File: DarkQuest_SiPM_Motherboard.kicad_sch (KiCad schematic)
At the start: 46 parts, among them J1 Conn_Coaxial, J10 Conn_Coaxial, J11 Conn_Coaxial, J12 Conn_Coaxial, J13 8-102202-4, J14 8-102202-4, J15 8-102202-4, J16 8-102202-4, J17 SiPM Chip Pin Header (K), J18 SiPM Chip Pin Header (K)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

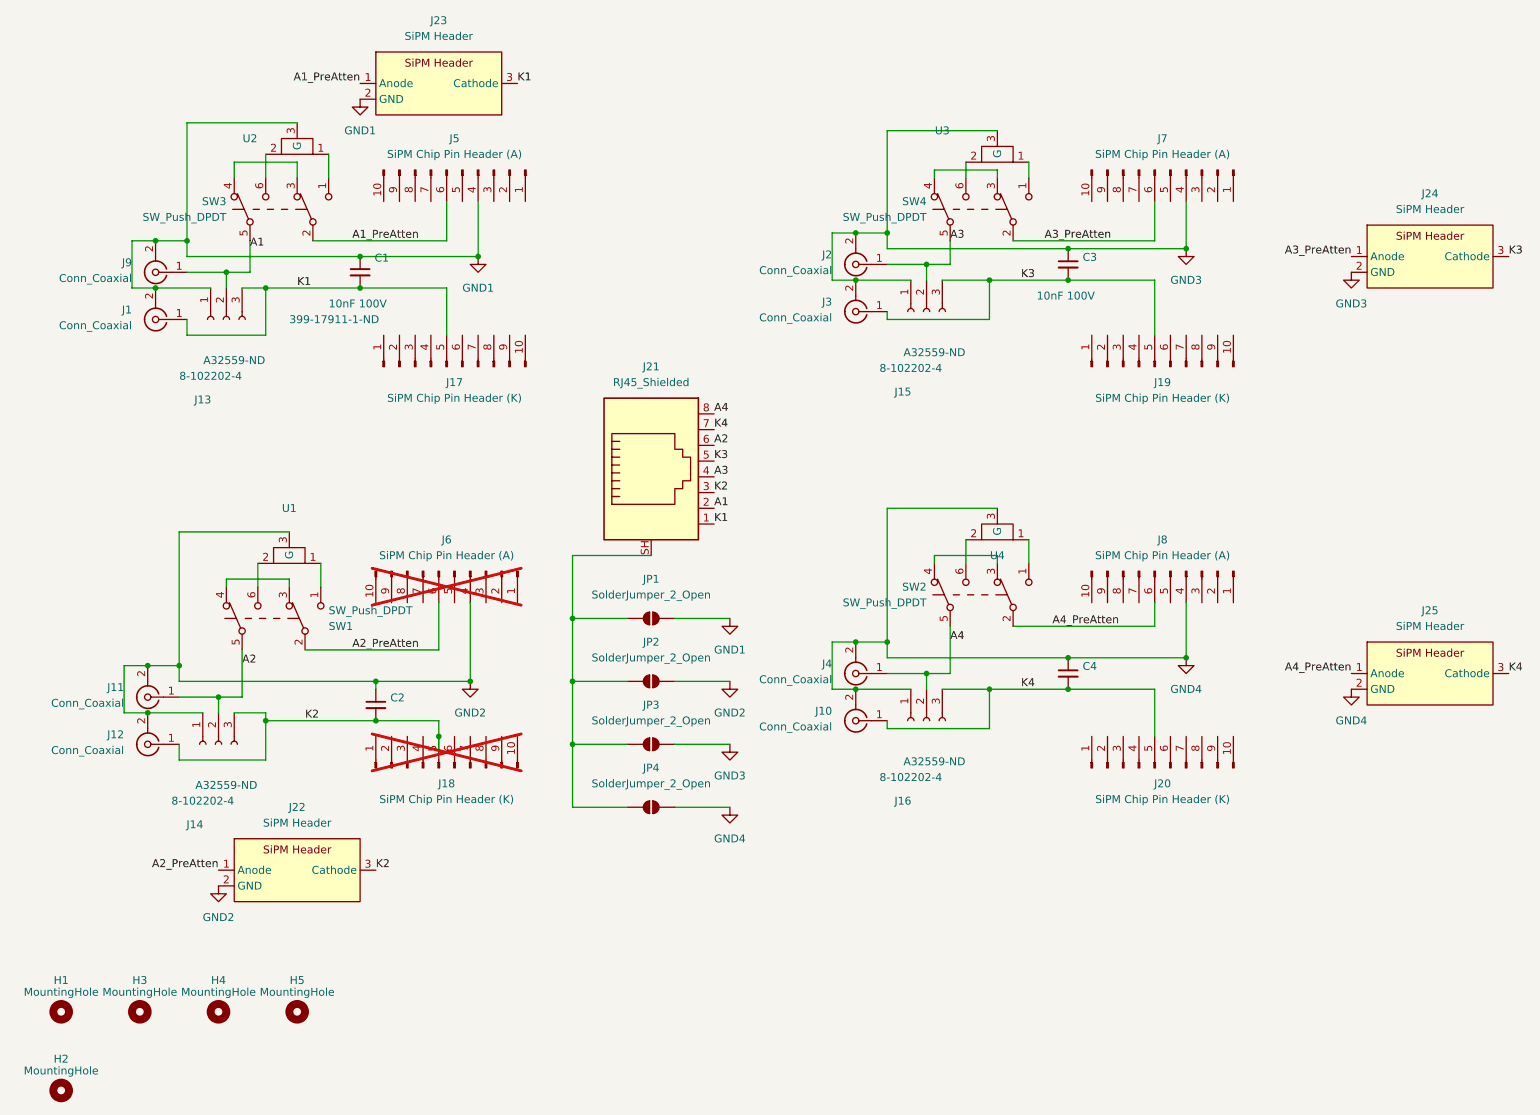
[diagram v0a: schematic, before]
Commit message: Added HDMI option
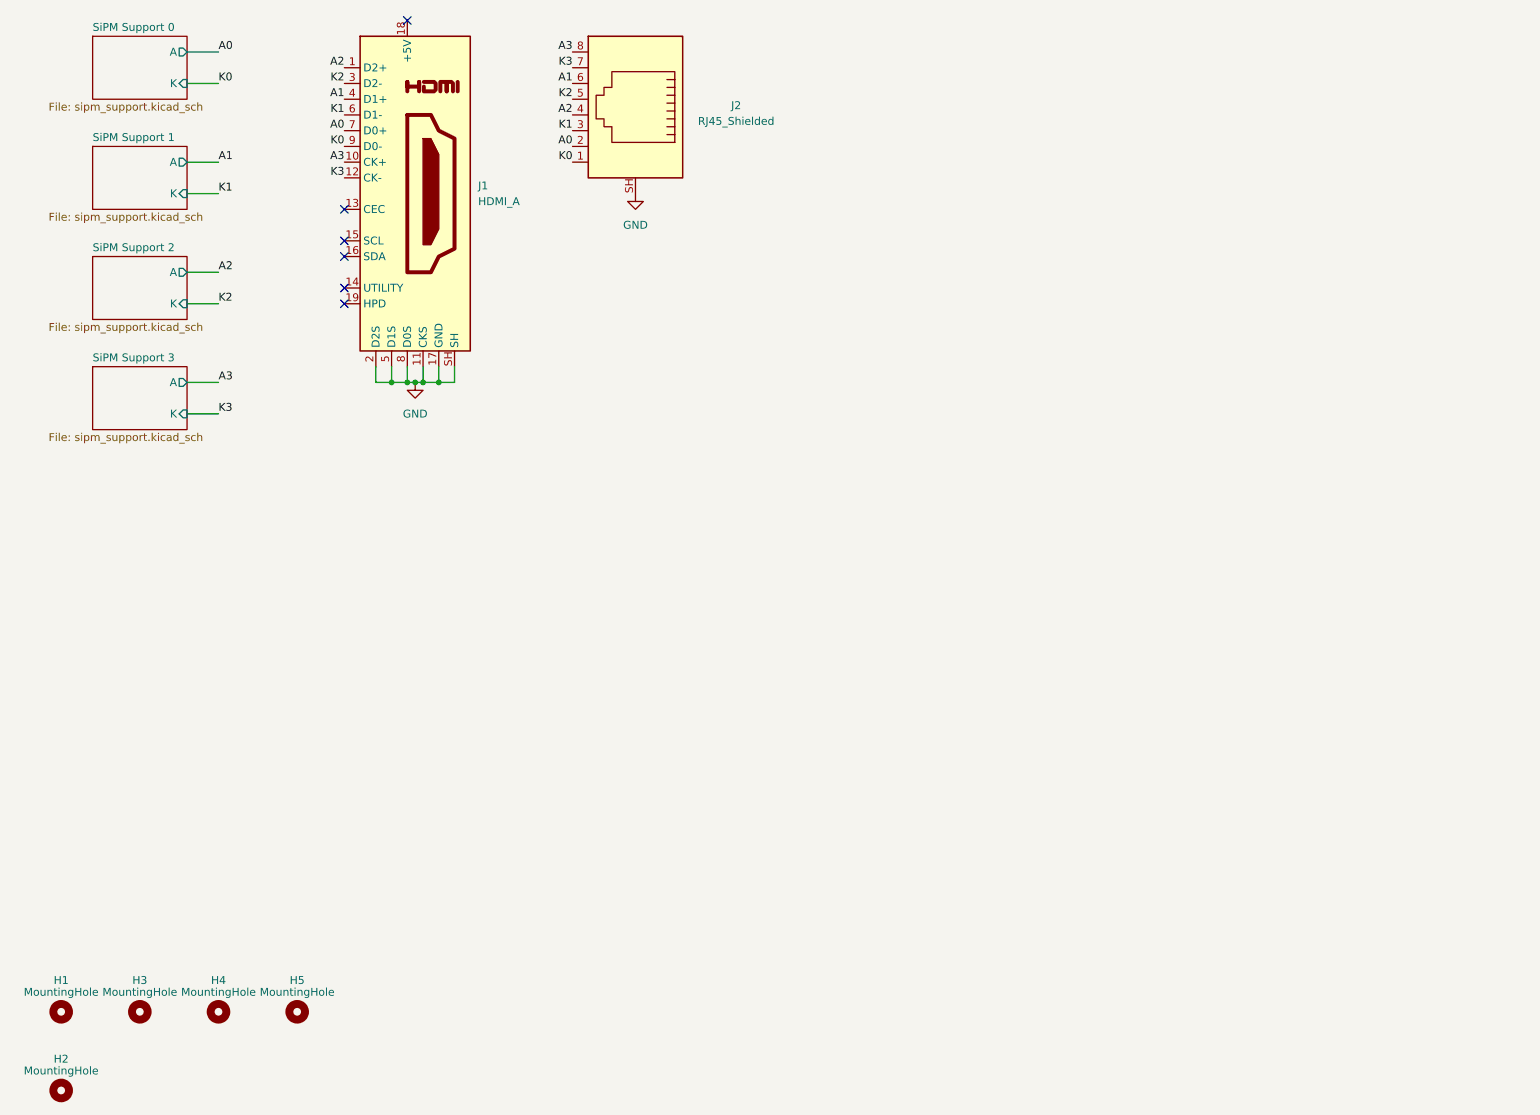
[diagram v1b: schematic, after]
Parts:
- removed C1, C2, C3, C4: 10nF 100V, Capacitor_SMD:C_1206_3216Metric_Pad1.33x1.80mm_HandSolder, symbol Device:C_Small
- removed J1, J10, J11, J12, J2, J3, J4, J9: Conn_Coaxial, Connector_Coaxial:WR-MMCX_Wuerth_66012102111404_Vertical, symbol Connector:Conn_Coaxial
- removed J13, J14, J15, J16: 8-102202-4, Connector_PinHeader_2.54mm:PinHeader_1x03_P2.54mm_Vertical, symbol Connector:Conn_01x03_Female
- removed J17, J18, J19, J20: SiPM Chip Pin Header (K), Connector_PinHeader_2.54mm:PinHeader_1x10_P2.54mm_Vertical, symbol Connector:Conn_01x10_Pin
- removed J22, J23, J24, J25: SiPM Header, RJJS-88-122-E7V-022:chip_carrier_pin_header, symbol SiPMConnector:SiPM_Header
- removed J5, J6, J7, J8: SiPM Chip Pin Header (A), Connector_PinHeader_2.54mm:PinHeader_1x10_P2.54mm_Vertical, symbol Connector:Conn_01x10_Pin
- removed JP1, JP2, JP3, JP4: SolderJumper_2_Open, Jumper:SolderJumper-2_P1.3mm_Open_RoundedPad1.0x1.5mm, symbol Jumper:SolderJumper_2_Open
- removed SW1, SW2, SW3, SW4: SW_Push_DPDT, Relay_SMD:Nidec_DPDT_CS422YTA, symbol Switch:Nidec_DPDT
- removed U1, U2, U3, U4: ~, Resistor_SMD:D10AA20Z4, symbol Analog:D10AA20Z4
- added J1: HDMI_A, symbol Connector:HDMI_A
- H1, H2, H3, H4, H5: now left out of the parts list
- J2: renamed from J21; DigiKey Part Number (none) -> 4414-3257-0005-02-ND
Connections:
- net A4 is gone; now on net A3: J2.8
- net K4 is gone; now on net K3: J2.7
- net A1: now also J2.6, J1.4 (D1+); no longer J2.2
- net A2: now also J2.4, J1.1 (D2+); no longer J2.6
- net A3: now also J1.10 (CK+); no longer J2.4
- net K1: now also J2.3, J1.6 (D1-); no longer J2.1
- net K2: now also J2.5, J1.3 (D2-); no longer J2.3
- net K3: now also J1.12 (CK-); no longer J2.5
- net GND: now reaches J2.SH
- net GND: now also J1.11 (CKS), J1.17 (GND), J1.2 (D2S), J1.5 (D1S), J1.8 (D0S), J1.SH
- new net A0: J1.7 (D0+), J2.2
- new net K0: J1.9 (D0-), J2.1
- no-connect marks 0 -> 6
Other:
- added sheet SiPM Support 0 (sipm_support.kicad_sch)
- added sheet SiPM Support 1 (sipm_support.kicad_sch)
- added sheet SiPM Support 2 (sipm_support.kicad_sch)
- added sheet SiPM Support 3 (sipm_support.kicad_sch)
- moved on the sheet: J2
